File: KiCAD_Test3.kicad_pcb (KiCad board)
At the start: 2 copper layers, 58.7 x 53.7 mm, 39 parts, among them J1 HDR_6_2.54, P1 PCIEx4 EDGE CONNECTOR, U1 ESP32-D0WDQ6, U2 TXB0104PWR, U3 IS25WP032D

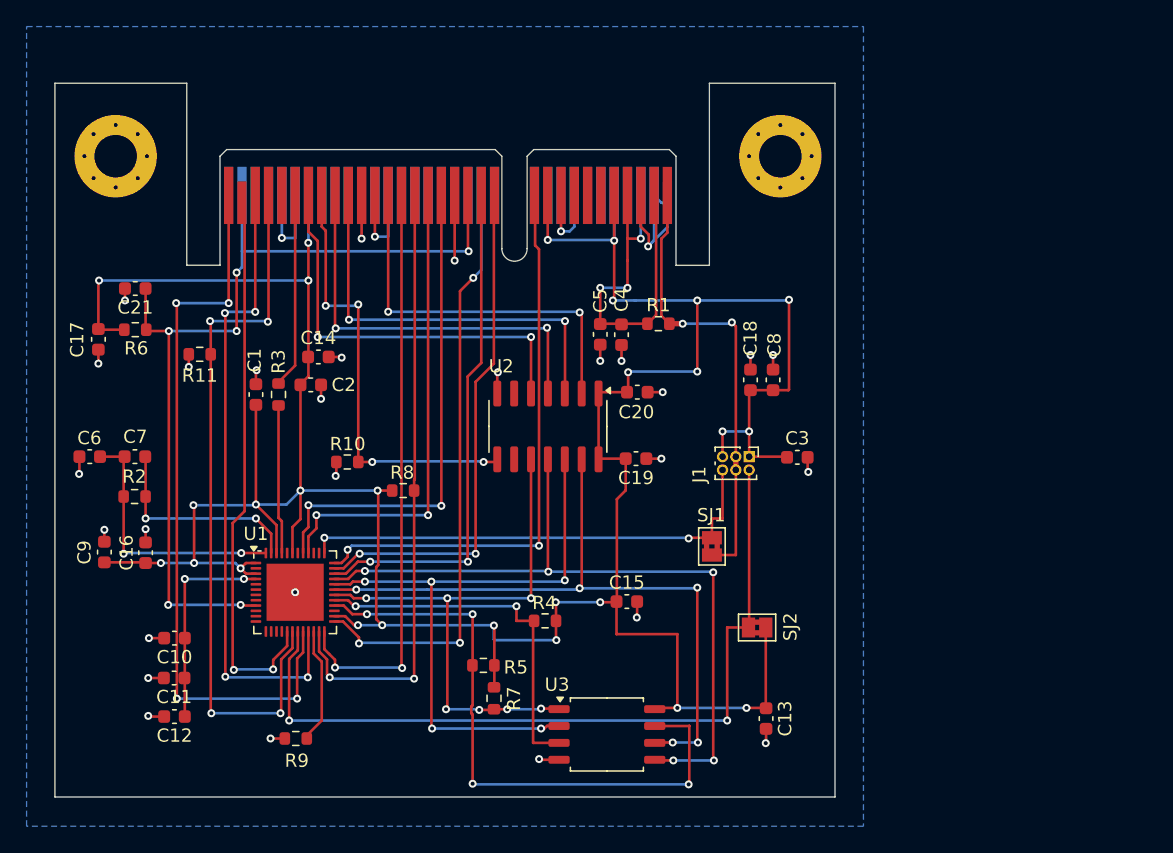
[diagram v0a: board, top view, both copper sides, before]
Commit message: updated ESP32 design - needs silkscreen added and shunt should be moved to be closer to U1
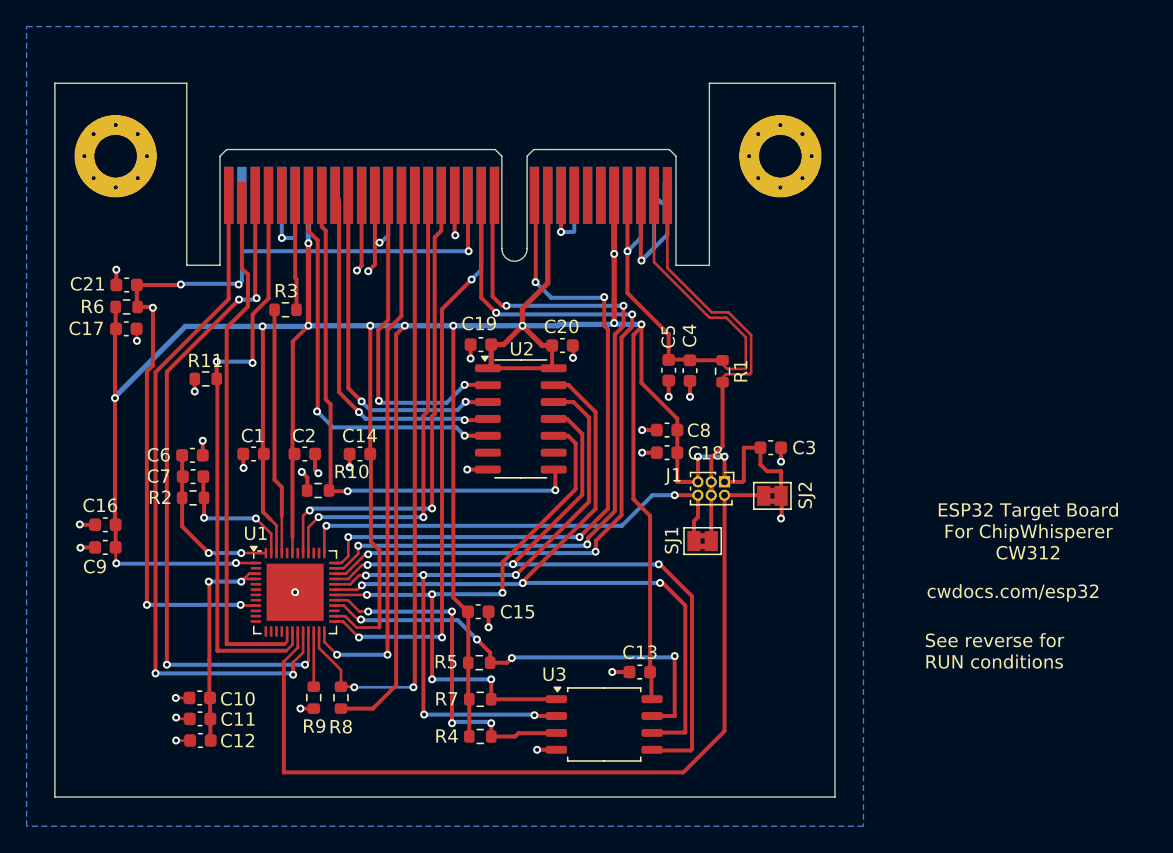
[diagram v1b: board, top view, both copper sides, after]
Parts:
- moved R8 16.3 mm to (146.0, 111.8), turned to -90 degrees
- moved C19 14.5 mm to (156.5, 85.3), turned to 180 degrees
- moved C15 11.2 mm to (156.3, 105.4)
- moved C13 10.1 mm to (168.5, 109.9), turned to 180 degrees
- moved R4 9.97 mm to (156.5, 114.8), turned to 180 degrees
- moved SJ2 9.97 mm to (178.4, 96.7)
- moved C8 8.82 mm to (170.5, 91.7), turned to 180 degrees
- moved C18 8.33 mm to (170.5, 93.4), turned to 180 degrees
- moved C14 7.94 mm to (147.4, 93.5), turned to 180 degrees
- moved C6 7.73 mm to (134.8, 93.6), turned to 180 degrees
- moved C20 6.64 mm to (162.7, 85.3)
- moved R3 6.40 mm to (141.8, 82.7), turned to 0 degrees
- moved R1 6.01 mm to (174.7, 87.3), turned to 90 degrees
- moved C5 5.81 mm to (170.7, 87.2)
- moved C4 5.81 mm to (172.2, 87.2)
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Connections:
- net /Sheet_1/BUF CS renamed /Connector/BUF CS
- net /Sheet_1/BUF SCK renamed /Connector/BUF SCK
- net /Sheet_1/BUF SDI renamed /Connector/BUF SDI
- net /Sheet_1/BUF SDO renamed /Connector/BUF SDO
- net /Sheet_1/CLK renamed /Connector/CLK
- net /Sheet_1/FLASH CS renamed /Integrated_Circuits/FLASH CS
- net /Sheet_1/FLASH HD renamed /Integrated_Circuits/FLASH HD
- net /Sheet_1/FLASH SCK renamed /Integrated_Circuits/FLASH SCK
- net /Sheet_1/FLASH SDI renamed /Integrated_Circuits/FLASH SDI
- net /Sheet_1/FLASH SDO renamed /Integrated_Circuits/FLASH SDO
- net /Sheet_1/FLASH WP renamed /Integrated_Circuits/FLASH WP
- net /Sheet_1/GPIO16 renamed /Connector/GPIO16
- net /Sheet_1/GPIO3 renamed /Connector/GPIO3
- net /Sheet_1/LED1 renamed /Connector/LED1
- net /Sheet_1/LED2 renamed /Connector/LED2
- net /Sheet_1/LED3 renamed /Connector/LED3
- net /Sheet_1/OE renamed /Connector/OE
- net /Sheet_1/RXD renamed /Connector/RXD
- net /Sheet_1/SHUNTH renamed /Connector/SHUNTH
- net /Sheet_1/SHUNTL renamed /Connector/SHUNTL
- net /Sheet_1/TCK renamed /Connector/TCK
- net /Sheet_1/TDI renamed /Connector/TDI
- net /Sheet_1/TDO renamed /Connector/TDO
- net /Sheet_1/TMS renamed /Connector/TMS
- net /Sheet_1/TRIG renamed /Connector/TRIG
- net /Sheet_1/TXD renamed /Connector/TXD
- net /Sheet_1/VDD CPU renamed /Integrated_Circuits/VDD CPU
- net /Sheet_1/VDD RTC renamed /Integrated_Circuits/VDD RTC
- net /Sheet_1/nRST renamed /Connector/nRST
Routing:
- net VCC: track 263.9 -> 331.8 mm, vias 29 -> 18
- net /Connector/LED3: track 38.4 -> 58.7 mm, vias 2 -> 4
- net /Connector/LED2: track 38.6 -> 57.0 mm, vias 2 -> 4
- net /Integrated_Circuits/FLASH HD: track 46.8 -> 34.5 mm
- net /Connector/SHUNTH: track 29.7 -> 41.7 mm, vias 3 -> 1
- net /Connector/TDI: track 55.2 -> 44.5 mm, vias 4 -> 2
- net /Connector/LED1: track 42.7 -> 51.3 mm, vias 2 -> 4
- net /Connector/OE: track 33.3 -> 41.2 mm, vias 4 -> 2
- net GND: track 70.5 -> 78.0 mm, vias 32 -> 33
- net Net-(U1-CAP1): track 19.9 -> 12.6 mm
- net Net-(U1-XTAL_P): track 11.2 -> 18.5 mm
- net /Integrated_Circuits/FLASH SCK: track 52.1 -> 58.5 mm, vias 5 -> 3
- net /Integrated_Circuits/VDD RTC: track 60.5 -> 66.4 mm, vias 2 -> 0
- net Net-(U1-CAP2): track 16.0 -> 10.1 mm
- net /Connector/CLK: track 14.4 -> 8.64 mm
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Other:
- board text added: "ESP32 Target Board For ChipWhisperer CW312"
- board text added: "See reverse for RUN conditions"
- board text added: "cwdocs.com/esp32"

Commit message: updated design for esp32
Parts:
- added PCB1: CE, Silkscrren_Symbols:CE-Logo_8.5x6mm_SilkScreen, F.Cu at (178.2, 104.6)
- added PCB2: Pb_Free, Silkscrren_Symbols:Pb_Free_8.0x8.0mm_SilkScreen, F.Cu at (176.8, 113.1)
- added PCB3: WEEE, Silkscrren_Symbols:WEEE-Logo_8.4x12mm_SilkScreen, F.Cu at (176.8, 94.0)
- moved SJ2 17.8 mm to (164.1, 107.2)
- moved C3 17.0 mm to (169.0, 107.2)
- moved R1 15.8 mm to (172.2, 102.8)
- moved J1 13.9 mm to (164.5, 104.8), turned to 180 degrees
- moved SJ1 13.4 mm to (160.2, 103.6), turned to -90 degrees
- moved C8 8.80 mm to (169.8, 100.5), turned to 90 degrees
- moved C18 7.48 mm to (168.1, 100.5), turned to 90 degrees
- moved C4 5.77 mm to (171.5, 92.9), turned to 180 degrees
- moved C5 4.25 mm to (171.5, 91.3), turned to 180 degrees
- moved R5 1.30 mm to (156.4, 110.5)
- moved C13 0.78 mm to (168.7, 110.7)
- moved U3 0.76 mm to (165.9, 114.6)
- moved R7 0.65 mm to (156.4, 112.6)
- moved R4 0.55 mm to (156.5, 115.3)
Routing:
- net VCC: track 331.8 -> 293.0 mm, vias 18 -> 17
- net /Connector/SHUNTH: track 41.7 -> 70.5 mm
- net /Integrated_Circuits/VDD RTC: track 66.4 -> 43.5 mm
- net /Connector/SHUNTL: track 32.1 -> 45.5 mm
- net GND: track 78.0 -> 87.0 mm
- net /Integrated_Circuits/FLASH SDI: track 57.6 -> 63.4 mm, vias 3 -> 5
- net /Integrated_Circuits/FLASH SCK: track 58.5 -> 64.0 mm
- net /Integrated_Circuits/FLASH CS: track 45.5 -> 49.3 mm, vias 5 -> 9
- net /Integrated_Circuits/FLASH SDO: track 51.7 -> 54.9 mm, vias 5 -> 7
- net /Integrated_Circuits/VDD CPU: track 34.7 -> 33.0 mm
- net /Connector/LED1: track 51.3 -> 50.4 mm
- net /Connector/nRST: track 69.6 -> 70.4 mm
- net /Connector/LED2: track 57.0 -> 56.3 mm
- net /Integrated_Circuits/FLASH WP: track 26.6 -> 27.1 mm, vias 4 -> 6
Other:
- board text added: "GPI00 (GPI03 on ChipWhisperer) 1 (HIGH) 0 (LOW)"
- board text added: "Mode RUN BOOTLDR"
- board text added: "NewAE Technology Inc. NAE-CW312T-ESP32 RoHS / Pb-Free"
- board text added: "Set PDIC (BUF_EN) high to enable SPI output"
- board text added: "Short TDI to GND to diable boot msgs."

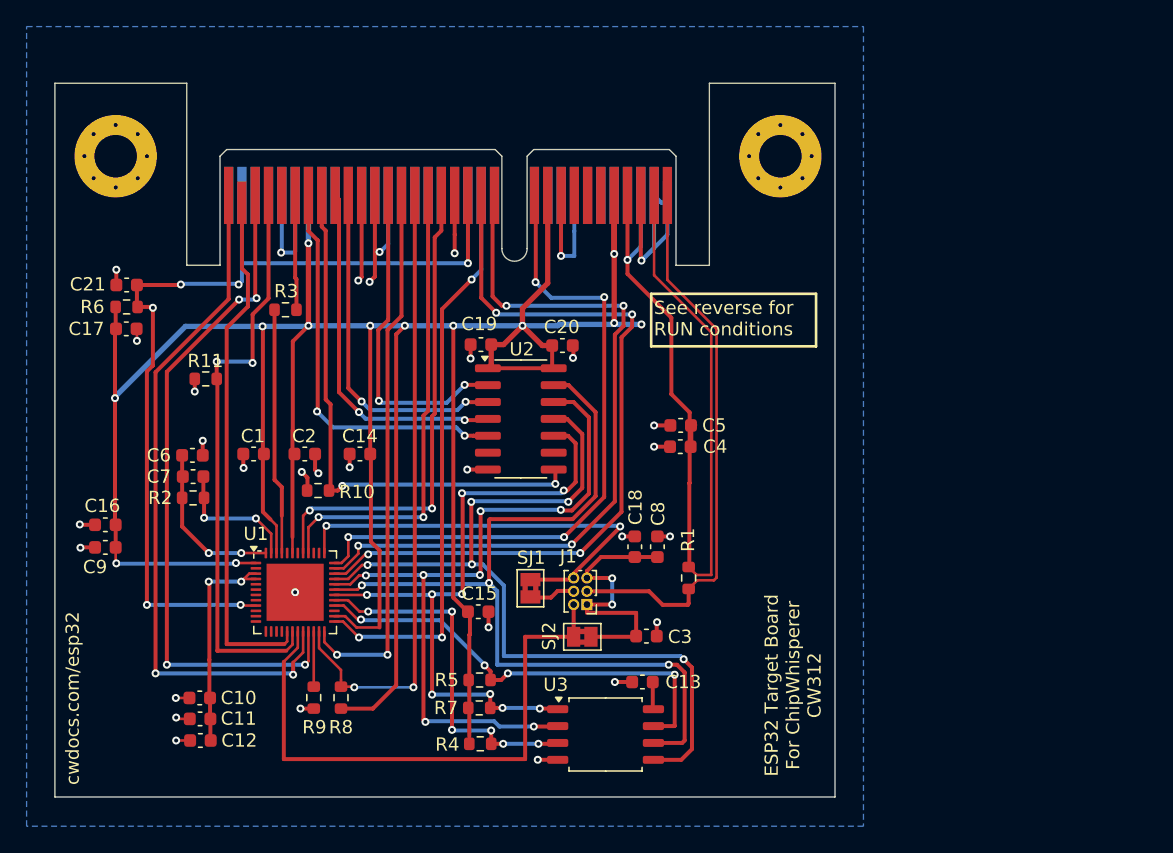
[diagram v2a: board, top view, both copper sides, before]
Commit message: updated design - removed visible pin numbers from passives, fixed connections, updated silkscreen
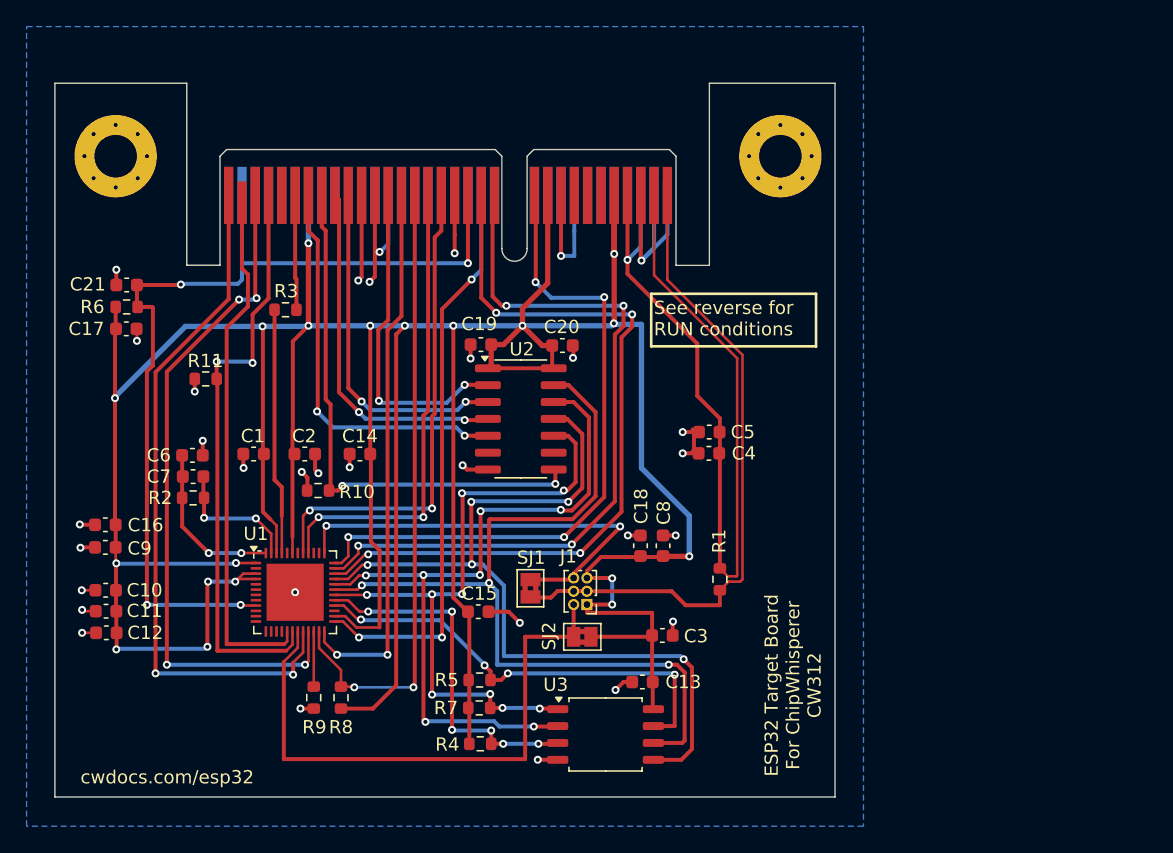
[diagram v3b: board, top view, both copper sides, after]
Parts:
- removed PCB1: CE, Silkscrren_Symbols:CE-Logo_8.5x6mm_SilkScreen
- removed PCB2: Pb_Free, Silkscrren_Symbols:Pb_Free_8.0x8.0mm_SilkScreen
- removed PCB3: WEEE, Silkscrren_Symbols:WEEE-Logo_8.4x12mm_SilkScreen
- added PCB4: UKCA symbol, Silkscrren_Symbols:UKCA-Logo_8x8mm_SilkScreen, F.Cu at (177.2, 95.1)
- added PCB5: CE Symbol, Silkscrren_Symbols:CE-Logo_8.5x6mm_SilkScreen, F.Cu at (178.1, 112.8)
- added PCB6: WEEE SYMBOL, Silkscrren_Symbols:WEEE-Logo_5.6x8mm_SilkScreen, F.Cu at (177.5, 84.6)
- added PCB7: Pb_Free Symbol, Silkscrren_Symbols:Pb_Free_8.0x8.0mm_SilkScreen, F.Cu at (176.9, 104.5)
- moved C11 10.8 mm to (128.3, 105.3)
- moved C12 10.8 mm to (128.3, 107.0)
- moved C10 10.8 mm to (128.3, 103.8)
- moved R1 2.35 mm to (174.5, 102.9)
- moved C4 2.21 mm to (173.7, 93.5)
- moved C5 2.21 mm to (173.7, 91.8)
- moved C3 1.20 mm to (170.2, 107.2)
- moved C18 0.43 mm to (168.5, 100.4)
- moved C8 0.43 mm to (170.2, 100.4)
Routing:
- net VCC: track 293.0 -> 326.9 mm, vias 17 -> 19
- net GND: track 87.0 -> 81.1 mm, vias 33 -> 32
- net /Connector/SHUNTL: track 45.5 -> 49.3 mm
- net /Connector/SHUNTH: track 70.5 -> 69.2 mm
- net /Connector/nRST: track 70.4 -> 70.3 mm, vias 6 -> 4
